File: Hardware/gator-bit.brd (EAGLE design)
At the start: 114.3 x 66 mm, 85 parts, among them J1 GATOR, J19 GATOR, J2 GATOR, J20 GATOR, J21 GATOR, J22 GATOR, J25 GATOR, J28 GATOR, J3 GATOR, J32 GATOR, J33 GATOR, J34 GATOR, J35 GATOR, J36 GATOR, J39 GATOR, J4 GATOR, J40 GATOR, J42 GATOR, U1 5V, U2 micro:bit, U4 MIC5219 3.3V

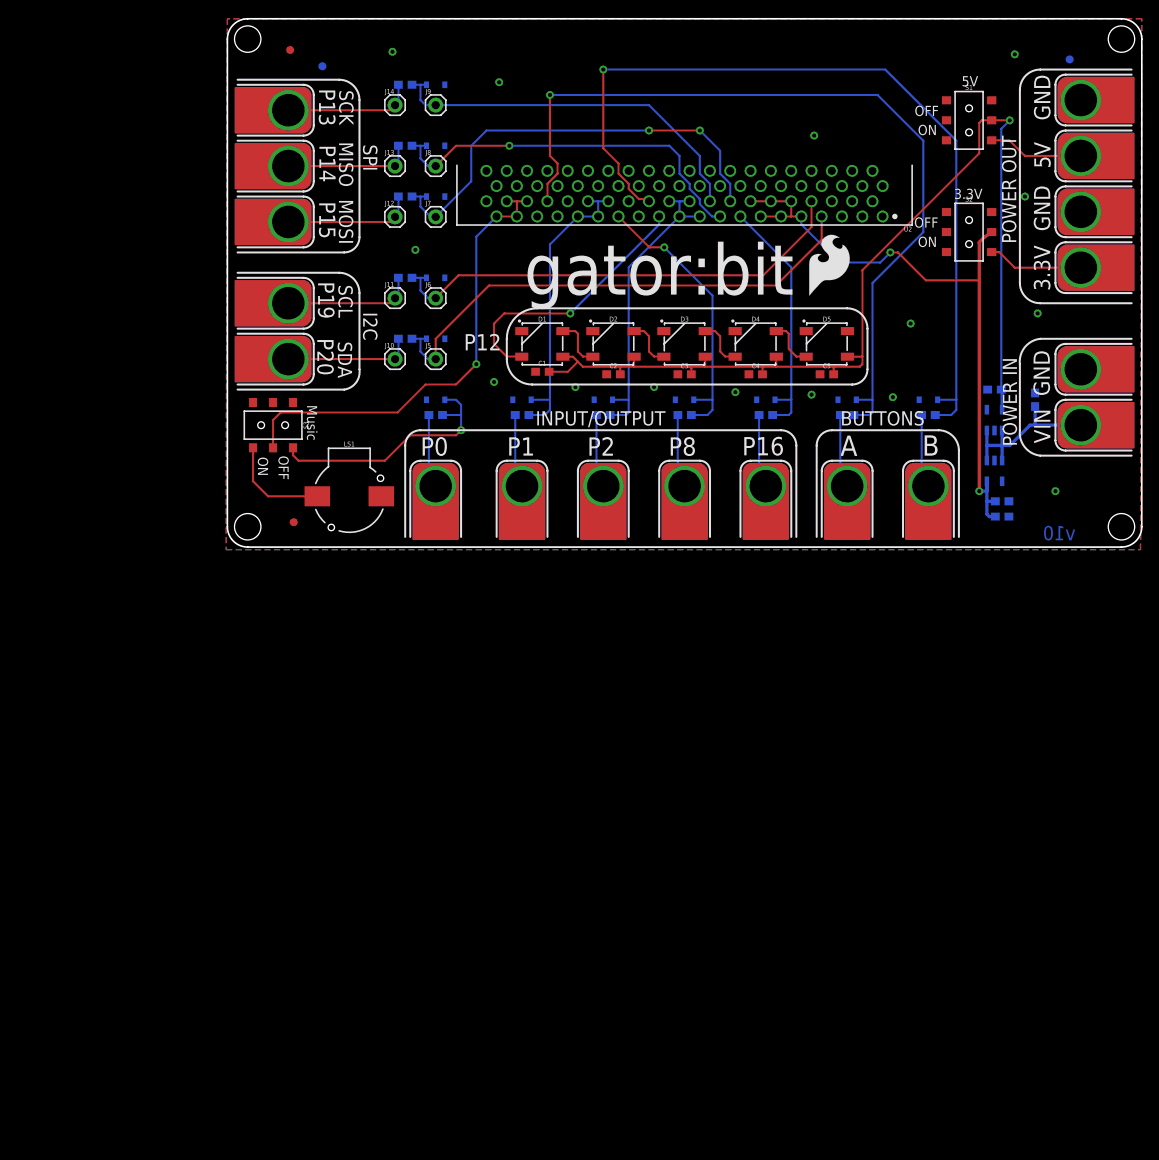
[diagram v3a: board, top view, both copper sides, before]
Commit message: Added a battery connector
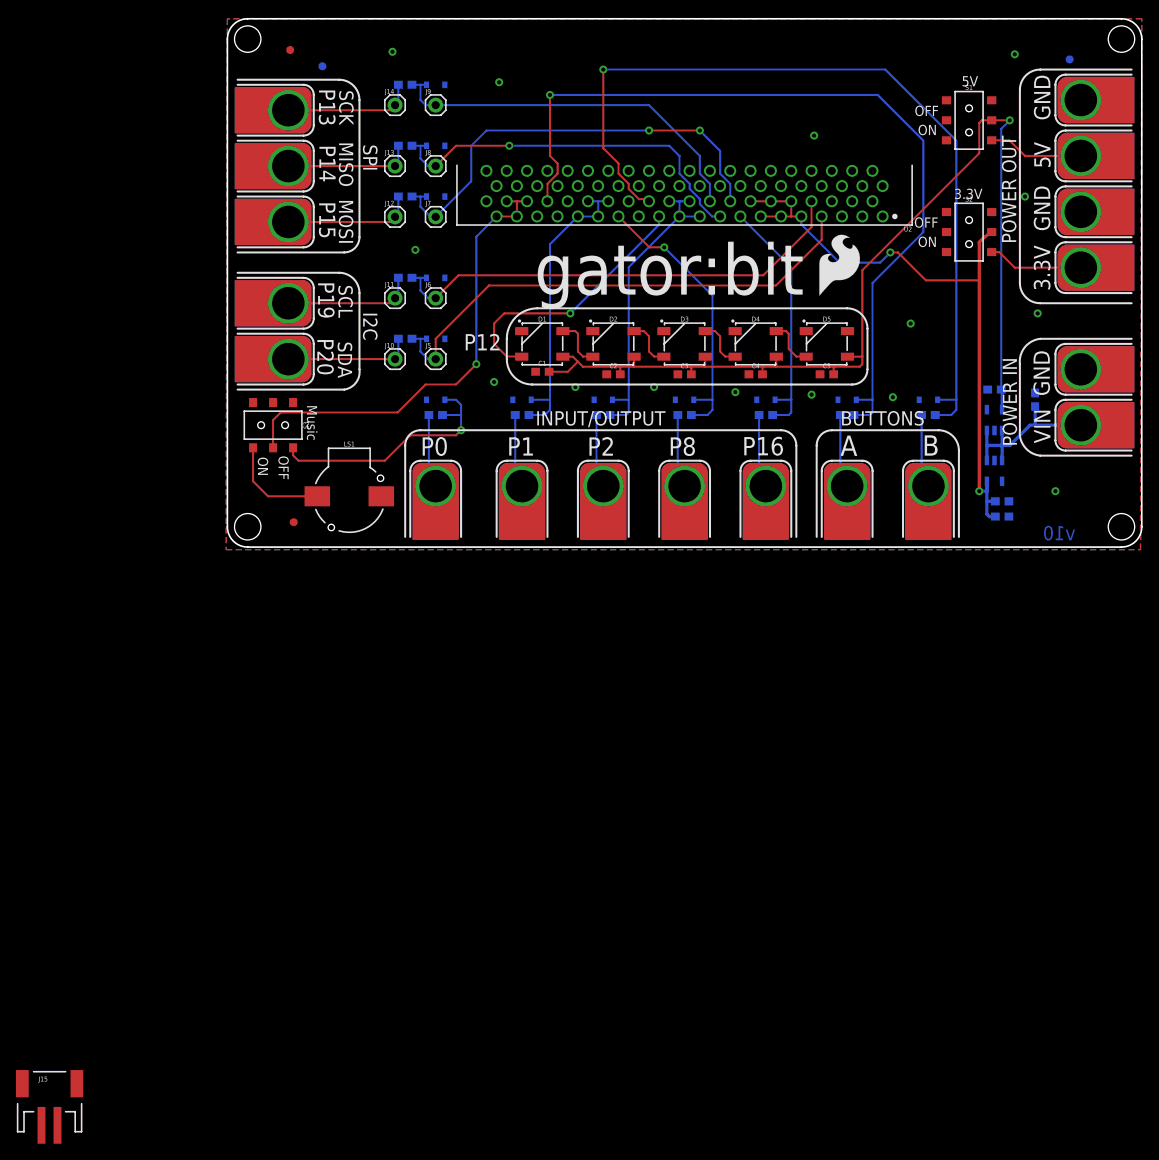
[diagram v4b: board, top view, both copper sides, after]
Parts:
- added J15: (no value), SparkFun-Connectors:JST-2-SMD
- moved LOGO1 1.27 mm to (73.5, 31.3)
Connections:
- net GND: now also J15.2
- net VIN: now also J15.1
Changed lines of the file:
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@@
 <dimension x1="2.54" y1="63.5" x2="0.79375" y2="63.5" x3="1.666875" y3="68.2625" textsize="1.778" layer="47" unit="inch"/>
 <text x="4.318" y="-40.64" size="2.54" layer="51">Solder Mask: Black Gloss</text>
-<text x="37.084" y="31.5595" size="6.35" layer="21">gator:bit</text>
+<text x="38.354" y="31.5595" size="6.35" layer="21">gator:bit</text>
 <dimension x1="114.3" y1="67.31" x2="57.15" y2="67.31" x3="85.725" y3="84.455" textsize="1.778" layer="47" unit="inch"/>
 <text x="24.129996875" y="11.43" size="2.286" layer="21" font="vector" ratio="15">P0</text>
@@
 <element name="J3" library="TAB" package="GATOR" value="GATOR" x="106.68" y="15.24" rot="R90"/>
 <element name="J4" library="TAB" package="GATOR" value="GATOR" x="106.68" y="22.225" rot="R90"/>
-<element name="LOGO1" library="SparkFun-Aesthetics" package="SFE_LOGO_FLAME_.3" value="SFE_LOGO_FLAME.3_INCH" x="72.228965625" y="31.26699375"/>
+<element name="LOGO1" library="SparkFun-Aesthetics" package="SFE_LOGO_FLAME_.3" value="SFE_LOGO_FLAME.3_INCH" x="73.498965625" y="31.26699375"/>
 <element name="LS1" library="SparkFun-Electromechanical" package="BUZZER-CCV" value="BUZZER-SMD" x="15.24" y="6.35" rot="R180">
 <attribute name="PROD_ID" value="COMP-08568" x="15.24" y="6.35" size="1.778" layer="27" rot="R180" display="off"/>
@@
 <element name="C9" library="SparkFun-Capacitors" package="0603-POLAR" value="10uF" x="100.965" y="18.415" rot="MR270">
 <attribute name="PROD_ID" value="CAP-13210" x="100.965" y="18.415" size="1.778" layer="28" rot="MR270" display="off"/>
+</element>
+<element name="J15" library="SparkFun-Connectors" package="JST-2-SMD" value="" x="-22.225" y="-68.58">
+<attribute name="PROD_ID" value="CONN-11443" x="-22.225" y="-68.58" size="1.778" layer="27" display="off"/>
 </element>
 </elements>
@@
 <via x="85.4075" y="27.94" extent="1-16" drill="0.508"/>
 <via x="103.505" y="6.985" extent="1-16" drill="0.508"/>
+<contactref element="J15" pad="2"/>
+<wire x1="98.425" y1="61.595" x2="106.68" y2="55.88" width="0" layer="19" extent="1-1"/>
+<wire x1="99.695" y1="43.815" x2="106.68" y2="55.88" width="0" layer="19" extent="1-1"/>
+<wire x1="106.68" y1="41.91" x2="99.695" y2="43.815" width="0" layer="19" extent="1-1"/>
+<wire x1="101.2825" y1="29.21" x2="106.68" y2="41.91" width="0" layer="19" extent="1-1"/>
+<wire x1="106.68" y1="22.225" x2="101.2825" y2="29.21" width="0" layer="19" extent="1-1"/>
+<wire x1="100.965" y1="19.265" x2="106.68" y2="22.225" width="0" layer="19" extent="16-16"/>
+<wire x1="95.035" y1="19.685" x2="100.965" y2="19.265" width="0" layer="19" extent="16-16"/>
+<wire x1="95.885" y1="14.5749" x2="95.035" y2="19.685" width="0" layer="19" extent="16-16"/>
+<wire x1="95.885" y1="10.8251" x2="95.885" y2="14.5749" width="0" layer="19" extent="16-16"/>
+<wire x1="97.6875" y1="5.715" x2="95.885" y2="10.8251" width="0" layer="19" extent="16-16"/>
+<wire x1="97.6875" y1="3.81" x2="97.6875" y2="5.715" width="0" layer="19" extent="16-16"/>
+<wire x1="103.505" y1="6.985" x2="97.6875" y2="5.715" width="0" layer="19" extent="16-16"/>
+<wire x1="86.48" y1="18.415" x2="95.035" y2="19.685" width="0" layer="19" extent="16-16"/>
+<wire x1="83.185" y1="18.7325" x2="86.48" y2="18.415" width="0" layer="19" extent="16-16"/>
+<wire x1="76.32" y1="18.415" x2="83.185" y2="18.7325" width="0" layer="19" extent="16-16"/>
+<wire x1="73.025" y1="19.05" x2="76.32" y2="18.415" width="0" layer="19" extent="16-16"/>
+<wire x1="74.08" y1="21.59" x2="73.025" y2="19.05" width="0" layer="19" extent="1-1"/>
+<wire x1="72.353" y1="27" x2="74.08" y2="21.59" width="0" layer="19" extent="1-1"/>
+<wire x1="66.16" y1="18.415" x2="73.025" y2="19.05" width="0" layer="19" extent="16-16"/>
+<wire x1="63.5" y1="19.3675" x2="66.16" y2="18.415" width="0" layer="19" extent="16-16"/>
+<wire x1="65.19" y1="21.59" x2="63.5" y2="19.3675" width="0" layer="19" extent="1-1"/>
+<wire x1="63.463" y1="27" x2="65.19" y2="21.59" width="0" layer="19" extent="1-1"/>
+<wire x1="56.3" y1="21.59" x2="63.5" y2="19.3675" width="0" layer="19" extent="1-1"/>
+<wire x1="56" y1="18.415" x2="56.3" y2="21.59" width="0" layer="19" extent="1-16"/>
+<wire x1="53.34" y1="20.0025" x2="56" y2="18.415" width="0" layer="19" extent="16-16"/>
+<wire x1="54.573" y1="27" x2="56.3" y2="21.59" width="0" layer="19" extent="1-1"/>
+<wire x1="47.41" y1="21.59" x2="53.34" y2="20.0025" width="0" layer="19" extent="1-1"/>
+<wire x1="45.84" y1="18.415" x2="47.41" y2="21.59" width="0" layer="19" extent="1-16"/>
+<wire x1="43.4975" y1="20.0025" x2="45.84" y2="18.415" width="0" layer="19" extent="16-16"/>
+<wire x1="38.52" y1="21.9075" x2="43.4975" y2="20.0025" width="0" layer="19" extent="1-1"/>
+<wire x1="35.68" y1="18.415" x2="38.52" y2="21.9075" width="0" layer="19" extent="1-16"/>
+<wire x1="33.3375" y1="20.6375" x2="35.68" y2="18.415" width="0" layer="19" extent="16-16"/>
+<wire x1="36.793" y1="27" x2="38.52" y2="21.9075" width="0" layer="19" extent="1-1"/>
+<wire x1="45.683" y1="27" x2="47.41" y2="21.59" width="0" layer="19" extent="1-1"/>
+<wire x1="27.185" y1="26.035" x2="33.3375" y2="20.6375" width="0" layer="19" extent="16-16"/>
+<wire x1="27.185" y1="33.655" x2="27.185" y2="26.035" width="0" layer="19" extent="16-16"/>
+<wire x1="24.885" y1="18.415" x2="27.185" y2="26.035" width="0" layer="19" extent="16-16"/>
+<wire x1="85.4075" y1="27.94" x2="83.185" y2="18.7325" width="0" layer="19" extent="1-1"/>
+<wire x1="27.185" y1="43.815" x2="27.185" y2="33.655" width="0" layer="19" extent="16-16"/>
+<wire x1="27.185" y1="50.165" x2="27.185" y2="43.815" width="0" layer="19" extent="16-16"/>
+<wire x1="27.185" y1="57.785" x2="27.185" y2="50.165" width="0" layer="19" extent="16-16"/>
+<wire x1="33.9725" y1="58.1025" x2="27.185" y2="57.785" width="0" layer="19" extent="16-16"/>
+<wire x1="20.6375" y1="61.9125" x2="27.185" y2="57.785" width="0" layer="19" extent="16-16"/>
+<wire x1="19.24" y1="6.35" x2="24.885" y2="18.415" width="0" layer="19" extent="1-16"/>
+<wire x1="81.9062375" y1="41.327525" x2="85.4075" y2="27.94" width="0" layer="19" extent="1-1"/>
+<wire x1="80.6362375" y1="43.227525" x2="81.9062375" y2="41.327525" width="0" layer="19" extent="1-1"/>
+<wire x1="79.3662375" y1="41.327525" x2="80.6362375" y2="43.227525" width="0" layer="19" extent="1-1"/>
+<wire x1="78.0962375" y1="43.227525" x2="79.3662375" y2="41.327525" width="0" layer="19" extent="1-1"/>
+<wire x1="76.8262375" y1="41.327525" x2="78.0962375" y2="43.227525" width="0" layer="19" extent="1-1"/>
+<wire x1="75.5562375" y1="43.227525" x2="76.8262375" y2="41.327525" width="0" layer="19" extent="1-1"/>
+<wire x1="73.3425" y1="51.435" x2="75.5562375" y2="43.227525" width="0" layer="19" extent="1-1"/>
+<wire x1="-21.225" y1="-72.28" x2="19.24" y2="6.35" width="0" layer="19" extent="1-1"/>
 </signal>
 <signal name="3.3V">
@@
 <wire x1="96.835" y1="12.6975" x2="96.8375" y2="12.7" width="0.4064" layer="16"/>
 <wire x1="100.965" y1="17.565" x2="100.965" y2="15.24" width="0.4064" layer="16"/>
+<contactref element="J15" pad="1"/>
+<wire x1="-23.225" y1="-72.28" x2="94.935" y2="10.8251" width="0" layer="19" extent="1-16"/>
 </signal>
 <signal name="VOUT3.3">

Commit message: Add JST battery connector
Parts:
- moved J15 145.3 mm to (102.2, 6.35), turned to 90 degrees
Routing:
- net VIN: track 22.6 -> 37.2 mm
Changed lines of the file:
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@@
 <attribute name="PROD_ID" value="CAP-13210" x="100.965" y="18.415" size="1.778" layer="28" rot="MR270" display="off"/>
 </element>
-<element name="J15" library="SparkFun-Connectors" package="JST-2-SMD" value="" x="-22.225" y="-68.58">
-<attribute name="PROD_ID" value="CONN-11443" x="-22.225" y="-68.58" size="1.778" layer="27" display="off"/>
+<element name="J15" library="SparkFun-Connectors" package="JST-2-SMD" value="" x="102.235" y="6.35" rot="R90">
+<attribute name="PROD_ID" value="CONN-11443" x="102.235" y="6.35" size="1.778" layer="27" rot="R90" display="off"/>
 </element>
 </elements>
@@
 <via x="101.2825" y="29.21" extent="1-16" drill="0.508"/>
 <via x="85.4075" y="27.94" extent="1-16" drill="0.508"/>
-<via x="103.505" y="6.985" extent="1-16" drill="0.508"/>
+<via x="101.6" y="5.715" extent="1-16" drill="0.508"/>
 <contactref element="J15" pad="2"/>
-<wire x1="98.425" y1="61.595" x2="106.68" y2="55.88" width="0" layer="19" extent="1-1"/>
-<wire x1="99.695" y1="43.815" x2="106.68" y2="55.88" width="0" layer="19" extent="1-1"/>
-<wire x1="106.68" y1="41.91" x2="99.695" y2="43.815" width="0" layer="19" extent="1-1"/>
-<wire x1="101.2825" y1="29.21" x2="106.68" y2="41.91" width="0" layer="19" extent="1-1"/>
-<wire x1="106.68" y1="22.225" x2="101.2825" y2="29.21" width="0" layer="19" extent="1-1"/>
-<wire x1="100.965" y1="19.265" x2="106.68" y2="22.225" width="0" layer="19" extent="16-16"/>
-<wire x1="95.035" y1="19.685" x2="100.965" y2="19.265" width="0" layer="19" extent="16-16"/>
-<wire x1="95.885" y1="14.5749" x2="95.035" y2="19.685" width="0" layer="19" extent="16-16"/>
-<wire x1="95.885" y1="10.8251" x2="95.885" y2="14.5749" width="0" layer="19" extent="16-16"/>
-<wire x1="97.6875" y1="5.715" x2="95.885" y2="10.8251" width="0" layer="19" extent="16-16"/>
-<wire x1="97.6875" y1="3.81" x2="97.6875" y2="5.715" width="0" layer="19" extent="16-16"/>
-<wire x1="103.505" y1="6.985" x2="97.6875" y2="5.715" width="0" layer="19" extent="16-16"/>
-<wire x1="86.48" y1="18.415" x2="95.035" y2="19.685" width="0" layer="19" extent="16-16"/>
-<wire x1="83.185" y1="18.7325" x2="86.48" y2="18.415" width="0" layer="19" extent="16-16"/>
-<wire x1="76.32" y1="18.415" x2="83.185" y2="18.7325" width="0" layer="19" extent="16-16"/>
-<wire x1="73.025" y1="19.05" x2="76.32" y2="18.415" width="0" layer="19" extent="16-16"/>
-<wire x1="74.08" y1="21.59" x2="73.025" y2="19.05" width="0" layer="19" extent="1-1"/>
-<wire x1="72.353" y1="27" x2="74.08" y2="21.59" width="0" layer="19" extent="1-1"/>
-<wire x1="66.16" y1="18.415" x2="73.025" y2="19.05" width="0" layer="19" extent="16-16"/>
-<wire x1="63.5" y1="19.3675" x2="66.16" y2="18.415" width="0" layer="19" extent="16-16"/>
-<wire x1="65.19" y1="21.59" x2="63.5" y2="19.3675" width="0" layer="19" extent="1-1"/>
-<wire x1="63.463" y1="27" x2="65.19" y2="21.59" width="0" layer="19" extent="1-1"/>
-<wire x1="56.3" y1="21.59" x2="63.5" y2="19.3675" width="0" layer="19" extent="1-1"/>
-<wire x1="56" y1="18.415" x2="56.3" y2="21.59" width="0" layer="19" extent="1-16"/>
-<wire x1="53.34" y1="20.0025" x2="56" y2="18.415" width="0" layer="19" extent="16-16"/>
-<wire x1="54.573" y1="27" x2="56.3" y2="21.59" width="0" layer="19" extent="1-1"/>
-<wire x1="47.41" y1="21.59" x2="53.34" y2="20.0025" width="0" layer="19" extent="1-1"/>
-<wire x1="45.84" y1="18.415" x2="47.41" y2="21.59" width="0" layer="19" extent="1-16"/>
-<wire x1="43.4975" y1="20.0025" x2="45.84" y2="18.415" width="0" layer="19" extent="16-16"/>
-<wire x1="38.52" y1="21.9075" x2="43.4975" y2="20.0025" width="0" layer="19" extent="1-1"/>
-<wire x1="35.68" y1="18.415" x2="38.52" y2="21.9075" width="0" layer="19" extent="1-16"/>
-<wire x1="33.3375" y1="20.6375" x2="35.68" y2="18.415" width="0" layer="19" extent="16-16"/>
-<wire x1="36.793" y1="27" x2="38.52" y2="21.9075" width="0" layer="19" extent="1-1"/>
-<wire x1="45.683" y1="27" x2="47.41" y2="21.59" width="0" layer="19" extent="1-1"/>
-<wire x1="27.185" y1="26.035" x2="33.3375" y2="20.6375" width="0" layer="19" extent="16-16"/>
-<wire x1="27.185" y1="33.655" x2="27.185" y2="26.035" width="0" layer="19" extent="16-16"/>
-<wire x1="24.885" y1="18.415" x2="27.185" y2="26.035" width="0" layer="19" extent="16-16"/>
-<wire x1="85.4075" y1="27.94" x2="83.185" y2="18.7325" width="0" layer="19" extent="1-1"/>
-<wire x1="27.185" y1="43.815" x2="27.185" y2="33.655" width="0" layer="19" extent="16-16"/>
-<wire x1="27.185" y1="50.165" x2="27.185" y2="43.815" width="0" layer="19" extent="16-16"/>
-<wire x1="27.185" y1="57.785" x2="27.185" y2="50.165" width="0" layer="19" extent="16-16"/>
-<wire x1="33.9725" y1="58.1025" x2="27.185" y2="57.785" width="0" layer="19" extent="16-16"/>
-<wire x1="20.6375" y1="61.9125" x2="27.185" y2="57.785" width="0" layer="19" extent="16-16"/>
-<wire x1="19.24" y1="6.35" x2="24.885" y2="18.415" width="0" layer="19" extent="1-16"/>
-<wire x1="81.9062375" y1="41.327525" x2="85.4075" y2="27.94" width="0" layer="19" extent="1-1"/>
-<wire x1="80.6362375" y1="43.227525" x2="81.9062375" y2="41.327525" width="0" layer="19" extent="1-1"/>
-<wire x1="79.3662375" y1="41.327525" x2="80.6362375" y2="43.227525" width="0" layer="19" extent="1-1"/>
-<wire x1="78.0962375" y1="43.227525" x2="79.3662375" y2="41.327525" width="0" layer="19" extent="1-1"/>
-<wire x1="76.8262375" y1="41.327525" x2="78.0962375" y2="43.227525" width="0" layer="19" extent="1-1"/>
-<wire x1="75.5562375" y1="43.227525" x2="76.8262375" y2="41.327525" width="0" layer="19" extent="1-1"/>
-<wire x1="73.3425" y1="51.435" x2="75.5562375" y2="43.227525" width="0" layer="19" extent="1-1"/>
-<wire x1="-21.225" y1="-72.28" x2="19.24" y2="6.35" width="0" layer="19" extent="1-1"/>
 </signal>
 <signal name="3.3V">
@@
 <wire x1="100.965" y1="17.565" x2="100.965" y2="15.24" width="0.4064" layer="16"/>
 <contactref element="J15" pad="1"/>
-<wire x1="-23.225" y1="-72.28" x2="94.935" y2="10.8251" width="0" layer="19" extent="1-16"/>
+<wire x1="105.935" y1="5.35" x2="108.855" y2="5.35" width="0.4064" layer="1"/>
+<wire x1="108.855" y1="5.35" x2="109.855" y2="6.35" width="0.4064" layer="1"/>
+<wire x1="109.855" y1="6.35" x2="109.855" y2="12.065" width="0.4064" layer="1"/>
+<wire x1="109.855" y1="12.065" x2="106.68" y2="15.24" width="0.4064" layer="1"/>
 </signal>
 <signal name="VOUT3.3">

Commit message: Updated design
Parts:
- removed C6: 10uF, SparkFun-Capacitors:0603-POLAR
- removed J1, J42: GATOR, TAB:GATOR
- removed S1: (no value), SparkFun-Switches:SWITCH_DPDT_SMD_AYZ0202
- removed U1: 5V, SparkFun-IC-Power:SOT23-5
- added S4: (no value), SparkFun-Switches:SWITCH_DPDT_SMD_AYZ0202
- moved C7 30.4 mm to (88.6, 34.9), flipped to the top, turned to 180 degrees
- moved C8 29.5 mm to (84.1, 30.5), flipped to the top, turned to 270 degrees
- moved U4 22.8 mm to (87.0, 30.5), flipped to the top, turned to 0 degrees
- moved C9 16.0 mm to (90.2, 30.2), flipped to the top
- moved S3 13.4 mm to (17.9, 9.64), turned to 270 degrees
- moved FD1 10.9 mm to (1.94, 12.0)
- moved J15 9.53 mm to (109.9, 12.1), turned to 270 degrees
- moved J2 8.91 mm to (106.0, 50.8)
- moved J4 8.91 mm to (106.0, 31.1)
- moved LS1 7.63 mm to (8.62, 10.1), turned to 315 degrees
- moved J19 7.01 mm to (106.0, 41.9)
- moved R1 6.63 mm to (32.4, 18.4), flipped to the top
- moved S2 6.48 mm to (91.4, 45.7), turned to 0 degrees
- moved J3 6.38 mm to (106.0, 21.6)
- moved J9 5.43 mm to (24.1, 60.3)
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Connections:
- removed net 5V: C1.2, C2.2, C3.2, C4.2, C5.2, C6.+, D1.1, D2.1, D3.1, D4.1, D5.1, S1.2, U1.5
- removed net VOUT5: J1.P$1, S1.3
- new net VIN_TAB: J3.P$1, S4.1
- new net V_BATT: J15.1, S4.3
- net 3.3V: now also C1.2, C2.2, C3.2, C4.2, C5.2, D1.1, D2.1, D3.1, D4.1, D5.1
- net GND: no longer C6.-, J42.P$1, U1.2
- net VIN: now also S4.2; no longer J15.1, J3.P$1, U1.1, U1.3
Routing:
- net 5V: track 128.8 -> 0.00 mm, vias 1 -> 0
- net 3.3V: track 80.9 -> 141.4 mm, vias 2 -> 0
- net P11: track 106.1 -> 54.6 mm, vias 1 -> 3
- net P5: track 104.3 -> 58.3 mm, vias 1 -> 6
- net P20: track 64.5 -> 87.6 mm, vias 0 -> 1
- net P8: track 35.4 -> 56.5 mm
- net V_BATT: track 0.00 -> 17.0 mm
- net VIN_TAB: track 0.00 -> 16.6 mm
- net PD: track 31.6 -> 15.6 mm, vias 1 -> 0
- net P19: track 59.6 -> 72.9 mm
- net P0: track 58.3 -> 46.1 mm, vias 1 -> 0
- net VOUT5: track 12.0 -> 0.00 mm
- net P19+: track 16.3 -> 22.0 mm
- net P0+: track 9.24 -> 13.5 mm
- net P14+: track 16.0 -> 20.3 mm
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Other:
- board text added: "3V-12V"
- board text added: "Batt"
- board text added: "Clip"
- board text added: "PWR"
- board text removed: "5V"
